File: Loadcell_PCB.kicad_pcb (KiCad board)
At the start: 2 copper layers, 57.5 x 74.6 mm, 53 parts, among them J1 USB_C_Receptacle_USB2.0, J2 Load cell side, J3 Micro_SD_Card, J4 GPS, Q1 S8550, SW1 RESET, U1 ATmega328P-M, U2 CH340C, U3 HX711, U4 74125, U5 LD1117S33TR_SOT223, Y1 16MHz

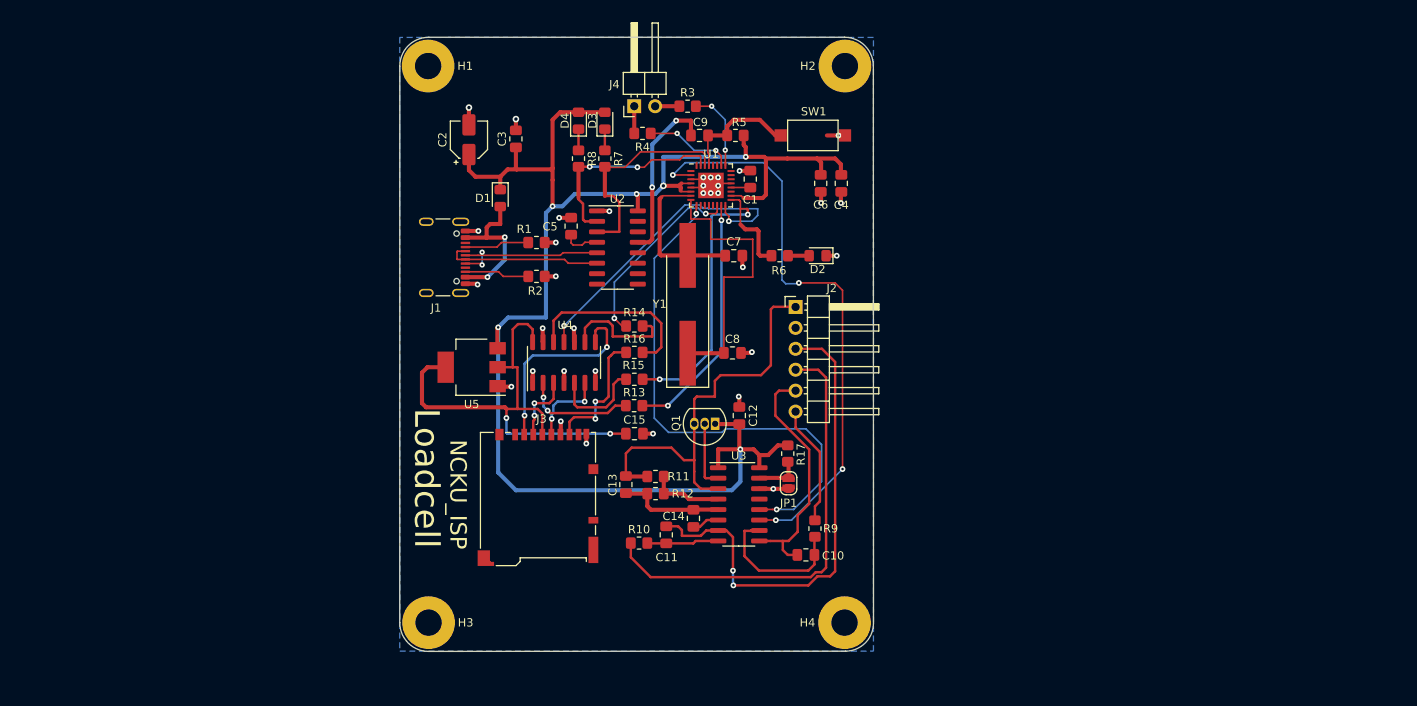
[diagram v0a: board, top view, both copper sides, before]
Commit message: Add new symbol and footprint for DC2DC converter
In order to power PT which requires 8V ~ 12V power supply, an 5V_12V
DC2DC converter in added into the schematic. Since the converter is
custom manufactured by an independent company, the correspond data
is not included in the Kicad library. So I have to draw it by my self.

Now, both symbol and footprint are finished, the next step is to
redraw the whole PCB layout and make it even more compact.
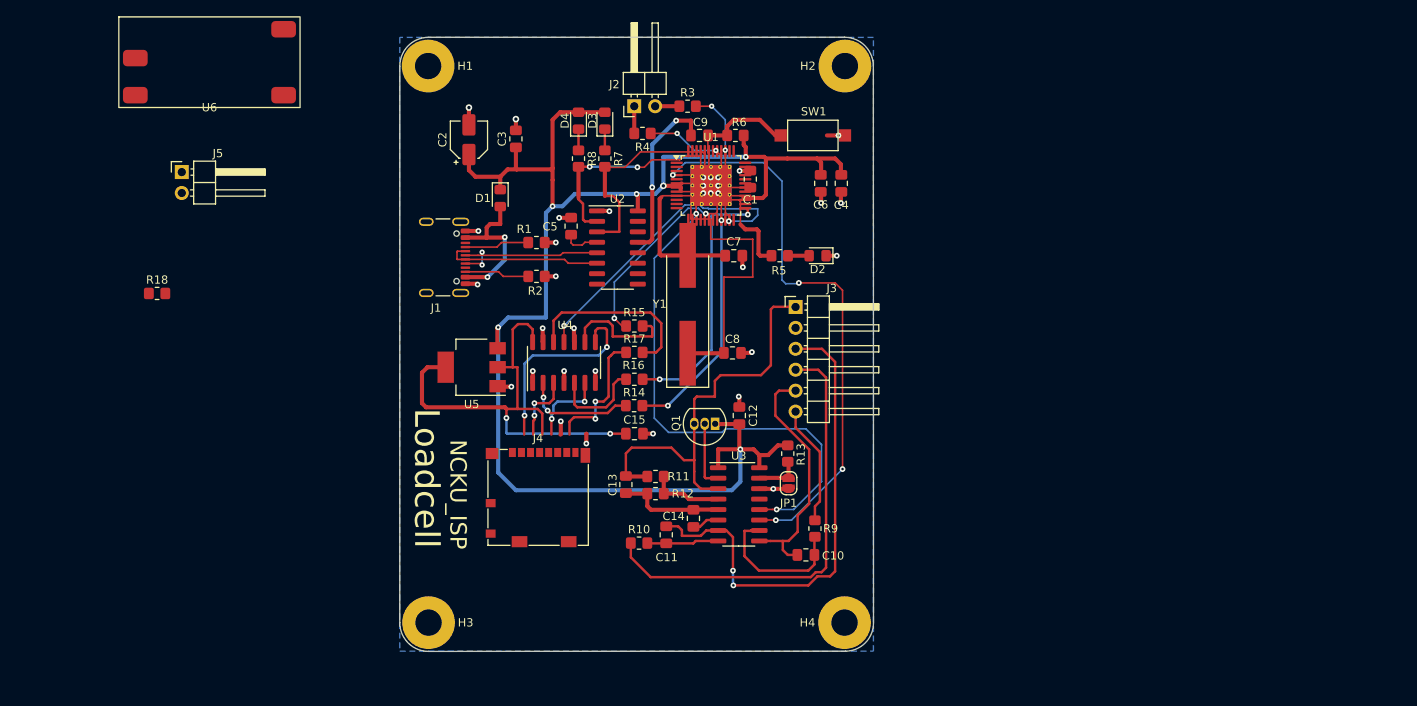
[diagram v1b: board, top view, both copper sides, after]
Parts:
- added J5: PT, Connector_PinHeader_2.54mm:PinHeader_1x02_P2.54mm_Horizontal, F.Cu at (46.0, 38.7)
- added R18: 250, Resistor_SMD:R_0805_2012Metric_Pad1.20x1.40mm_HandSolder, F.Cu at (43.0, 53.5)
- added U6: ~, Custom_footprints:DC2DC, F.Cu at (49.4, 24.9)
- C2: value 4u7F_16V -> 4.7uF_16V
- J4: renamed from J3; footprint Connector_Card:microSD_HC_Hirose_DM3BT-DSF-PEJS -> Connector_Card:microSD_HC_Molex_104031-0811
- U1: footprint Package_DFN_QFN:QFN-32-1EP_5x5mm_P0.5mm_EP3.1x3.1mm -> Package_QFP:TQFP-48-1EP_7x7mm_P0.5mm_EP5x5mm_ThermalVias
- renumbered J4 to J2, J2 to J3, R17 to R13, R13 to R14, R14 to R15, R15 to R16, R16 to R17, R6 to R5, R5 to R6
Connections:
- U1 pad 23: unconnected-(U1-PC0-Pad23) -> /PT_OUT

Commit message: Add new SD card slot 3D cad and start re-laying the PCB
New SD card slot has also no 3D cad in standard library, so I added
one. Also, new layout has started, and this commit is a save record
in case the app crashes which happens quite frequently at version 8.
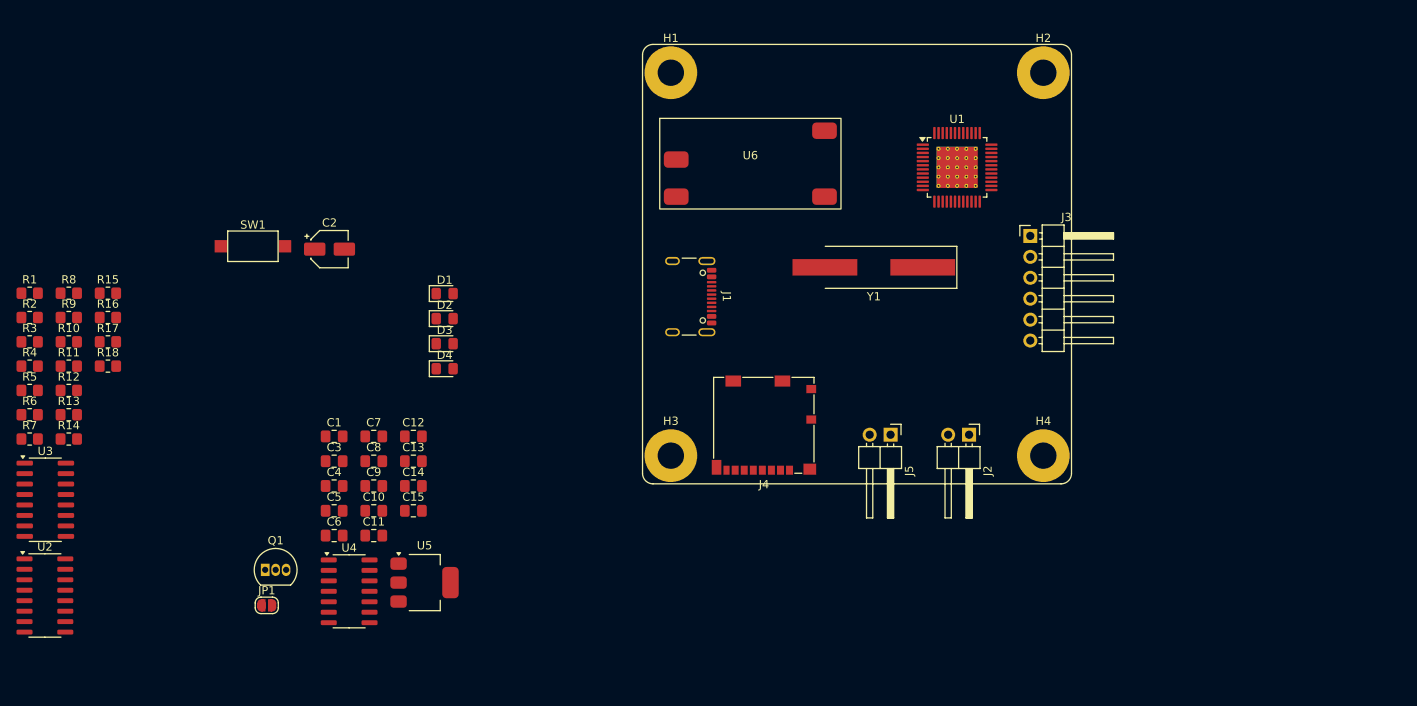
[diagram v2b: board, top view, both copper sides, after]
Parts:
- moved R9 94.1 mm to (32.3, 56.4), turned to 0 degrees
- moved R5 92.5 mm to (27.6, 65.2)
- moved R6 92.1 mm to (27.6, 68.2)
- moved J5 91.8 mm to (132.1, 70.6), turned to -90 degrees
- moved R13 87.4 mm to (32.3, 68.2), turned to 0 degrees
- moved R3 84.8 mm to (27.6, 59.3), turned to 0 degrees
- moved U3 84.2 mm to (29.5, 78.5)
- moved U2 81.3 mm to (29.4, 90.1)
- moved R4 79.6 mm to (27.6, 62.3), turned to 0 degrees
- moved R7 77.7 mm to (27.6, 71.1), turned to 0 degrees
- moved R10 73.4 mm to (32.3, 59.3)
- moved C6 72.9 mm to (64.5, 82.9), turned to 0 degrees
- moved R11 72.5 mm to (32.3, 62.3)
- moved R12 72.3 mm to (32.3, 65.2)
- moved C4 71.7 mm to (64.5, 76.8), turned to 0 degrees
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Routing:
- net +5V: track 190.9 -> 0.00 mm, vias 6 -> 0
- net /SCK: track 71.3 -> 0.00 mm, vias 4 -> 0
- net /DT: track 63.4 -> 0.00 mm, vias 2 -> 0
- net /SD_VCC: track 59.4 -> 0.00 mm, vias 2 -> 0
- net Net-(J3-Pin_3): track 59.4 -> 0.00 mm, vias 2 -> 0
- net Net-(J3-Pin_4): track 54.1 -> 0.00 mm
- net Net-(J3-Pin_1): track 50.1 -> 0.00 mm
- net GND: track 47.8 -> 0.00 mm, vias 34 -> 0
- net /SD_SCK: track 43.1 -> 0.00 mm, vias 2 -> 0
- net /MISO: track 38.4 -> 0.00 mm, vias 2 -> 0
- net Net-(U1-XTAL2/PB7): track 34.0 -> 0.00 mm
- net /MOSI: track 30.1 -> 0.00 mm, vias 2 -> 0
- net Net-(J3-Pin_5): track 29.8 -> 0.00 mm
- net /TX: track 26.3 -> 0.00 mm
- net /RX: track 24.9 -> 0.00 mm, vias 2 -> 0
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- removed copper zone on B.Cu, net GND
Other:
- board outline removed
- board text removed: "Loadcell"
- board text removed: "NCKU_ISP"

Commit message: Add PT reading function into loadcell program, waiting for test
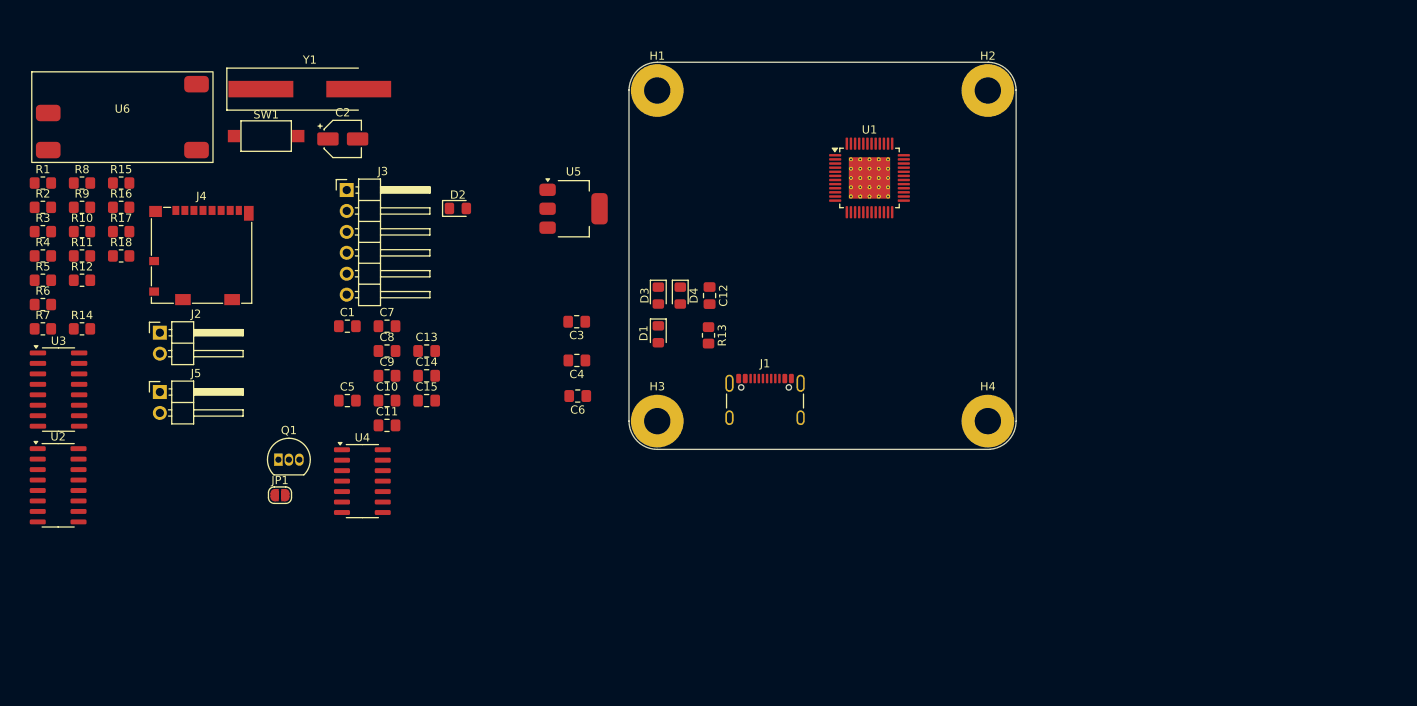
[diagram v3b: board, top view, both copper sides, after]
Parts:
- moved J2 99.0 mm to (43.4, 58.2), turned to 0 degrees
- moved J5 88.8 mm to (43.4, 65.4), turned to 0 degrees
- moved J3 83.2 mm to (66.1, 40.9)
- moved R13 78.3 mm to (110.0, 58.5), turned to -90 degrees
- moved U6 76.4 mm to (38.8, 31.6)
- moved Y1 71.8 mm to (61.6, 28.7), turned to 0 degrees
- moved J4 71.3 mm to (48.4, 48.8), turned to 0 degrees
- moved U5 48.9 mm to (93.6, 43.2)
- moved C12 39.8 mm to (110.1, 53.7), turned to -90 degrees
- moved C6 34.1 mm to (94.1, 65.9), turned to 180 degrees
- moved C3 34.0 mm to (94.0, 56.9)
- moved C4 33.2 mm to (94.0, 61.6), turned to 180 degrees
- moved D4 29.9 mm to (106.6, 53.7), turned to -90 degrees
- moved D3 26.6 mm to (103.9, 53.7), turned to -90 degrees
- moved D1 26.4 mm to (103.9, 58.4), turned to -90 degrees
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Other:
- board outline added: 47 x 47 mm

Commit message: Re-layout progress at 15% and add connector pin for in system programming
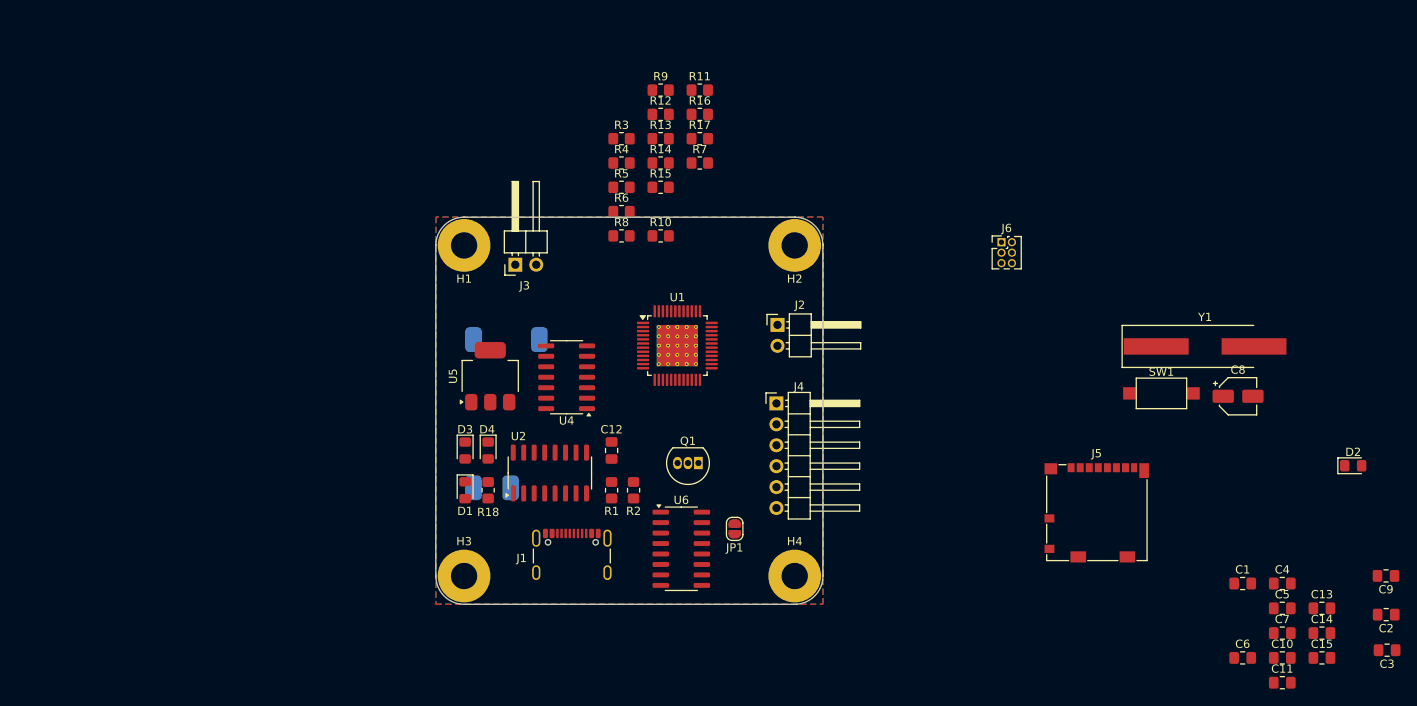
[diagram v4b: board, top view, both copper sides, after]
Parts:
- added J6: ISP, Connector_PinHeader_1.27mm:PinHeader_2x03_P1.27mm_Vertical, F.Cu at (145.5, 47.2)
- U3: renamed from U6; moved to B.Cu
- moved C8 113.1 mm to (174.3, 65.9)
- moved D2 113.1 mm to (188.2, 74.4)
- moved SW1 113.1 mm to (165.0, 65.6)
- moved Y1 113.1 mm to (170.3, 59.9)
- moved C10 113.1 mm to (179.6, 97.7)
- moved C11 113.1 mm to (179.6, 100.7)
- moved C13 113.1 mm to (184.4, 91.7)
- moved C14 113.1 mm to (184.4, 94.7)
- moved C15 113.1 mm to (184.4, 97.7)
- moved C4 113.1 mm to (179.6, 88.7)
- moved C5 113.1 mm to (179.6, 91.7)
- moved C7 113.1 mm to (179.6, 94.7)
- moved C1 113.1 mm to (174.8, 88.7)
- moved C6 113.1 mm to (174.8, 97.7)
- moved J5 113.1 mm to (157.1, 80.1)
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- renumbered C4 to C2, C6 to C3, C7 to C4, C8 to C5, C5 to C6, C9 to C7, C2 to C8, C3 to C9, J5 to J2, J2 to J3, J3 to J4, J4 to J5, R14 to R10, R15 to R11, R9 to R12, R10 to R13, R11 to R14, R12 to R15, R13 to R18, R18 to R7, R7 to R8, R8 to R9, U3 to U6
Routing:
- added copper zone on B.Cu, net GND
- added copper zone on F.Cu, net GND

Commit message: Change PT formula for 1.1V analogRead
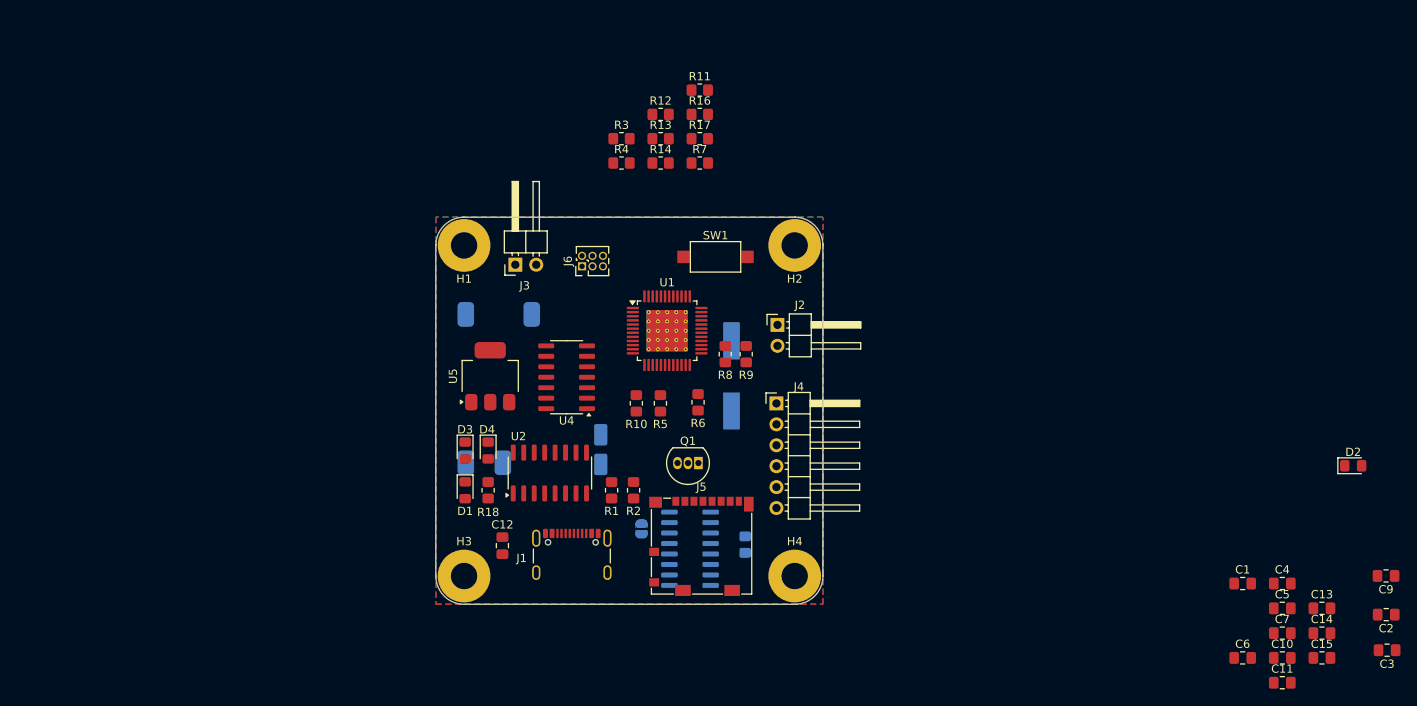
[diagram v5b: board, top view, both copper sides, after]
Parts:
- C8, JP1, R15, U6: moved to B.Cu
- Y1: footprint Crystal:Crystal_SMD_HC49-SD_HandSoldering -> Crystal:Crystal_SMD_HC49-SD; moved to B.Cu
- moved C8 77.6 mm to (96.9, 72.4), turned to 90 degrees
- moved Y1 57.6 mm to (112.8, 63.5), turned to 90 degrees
- moved SW1 56.6 mm to (110.8, 49.0)
- moved J6 51.0 mm to (94.6, 50.2), turned to 90 degrees
- moved J5 48.2 mm to (109.1, 84.1)
- moved R15 44.6 mm to (114.4, 83.9), turned to 90 degrees
- moved R9 33.7 mm to (114.6, 60.8), turned to 90 degrees
- moved R5 26.6 mm to (104.1, 66.8), turned to 90 degrees
- moved R6 24.9 mm to (108.7, 66.7), turned to -90 degrees
- moved R10 20.5 mm to (101.2, 66.8), turned to -90 degrees
- moved R8 19.1 mm to (112.0, 60.8), turned to 90 degrees
- moved C12 17.6 mm to (85.0, 84.1), turned to 90 degrees
- moved JP1 11.3 mm to (101.9, 82.0)
- moved U3 3.20 mm to (85.0, 65.0)
- moved U1 2.19 mm to (105.0, 58.0)
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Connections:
- J6 pad 1: unconnected-(J6-Pin_1-Pad1) -> /MISO
- J6 pad 2: unconnected-(J6-Pin_2-Pad2) -> /SD_SCK
- J6 pad 3: unconnected-(J6-Pin_3-Pad3) -> /RESET
- J6 pad 4: unconnected-(J6-Pin_4-Pad4) -> GND
- J6 pad 5: unconnected-(J6-Pin_5-Pad5) -> /MOSI
- J6 pad 6: unconnected-(J6-Pin_6-Pad6) -> /5V

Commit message: Update PCB conventionally
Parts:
- C11, C13, C14, C2, C3, C4, C5, R12, R14, R3, R4, R7: moved to B.Cu
- moved C2 112.6 mm to (80.4, 79.5), turned to 90 degrees
- moved C9 112.3 mm to (80.4, 77.0), turned to -90 degrees
- moved C3 110.5 mm to (83.2, 79.4), turned to 90 degrees
- moved C7 91.8 mm to (91.1, 70.4)
- moved C4 91.5 mm to (95.1, 53.7), turned to 180 degrees
- moved C6 87.5 mm to (89.1, 80.3)
- moved C15 87.0 mm to (101.7, 70.8), turned to 180 degrees
- moved D2 86.0 mm to (102.6, 66.8), turned to 90 degrees
- moved C5 84.2 mm to (98.7, 68.6), turned to -90 degrees
- moved C1 72.3 mm to (106.7, 64.5)
- moved C11 71.7 mm to (113.9, 72.0), turned to 180 degrees
- moved C14 71.7 mm to (113.2, 86.6), turned to 180 degrees
- moved C13 70.5 mm to (114.4, 83.3), turned to 90 degrees
- moved C10 69.2 mm to (114.1, 75.6)
- moved R12 47.9 mm to (113.6, 78.7)
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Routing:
- net +5V: track 0.00 -> 103.5 mm, vias 0 -> 1
- net /VUSB: track 0.00 -> 14.0 mm
